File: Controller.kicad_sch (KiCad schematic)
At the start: 33 parts, among them J12 Conn_01x03_Pin, J2 Conn_01x04_Pin, J3 Conn_01x02_Pin, J4 Conn_01x02_Pin, J5 Conn_01x04_Pin, J6 Conn_01x02_Pin, SW1 SW_Push, U1 STM32F407VETx, U6 TL431M-0.3%-6AF, Y1 8M, Y2 32.768K

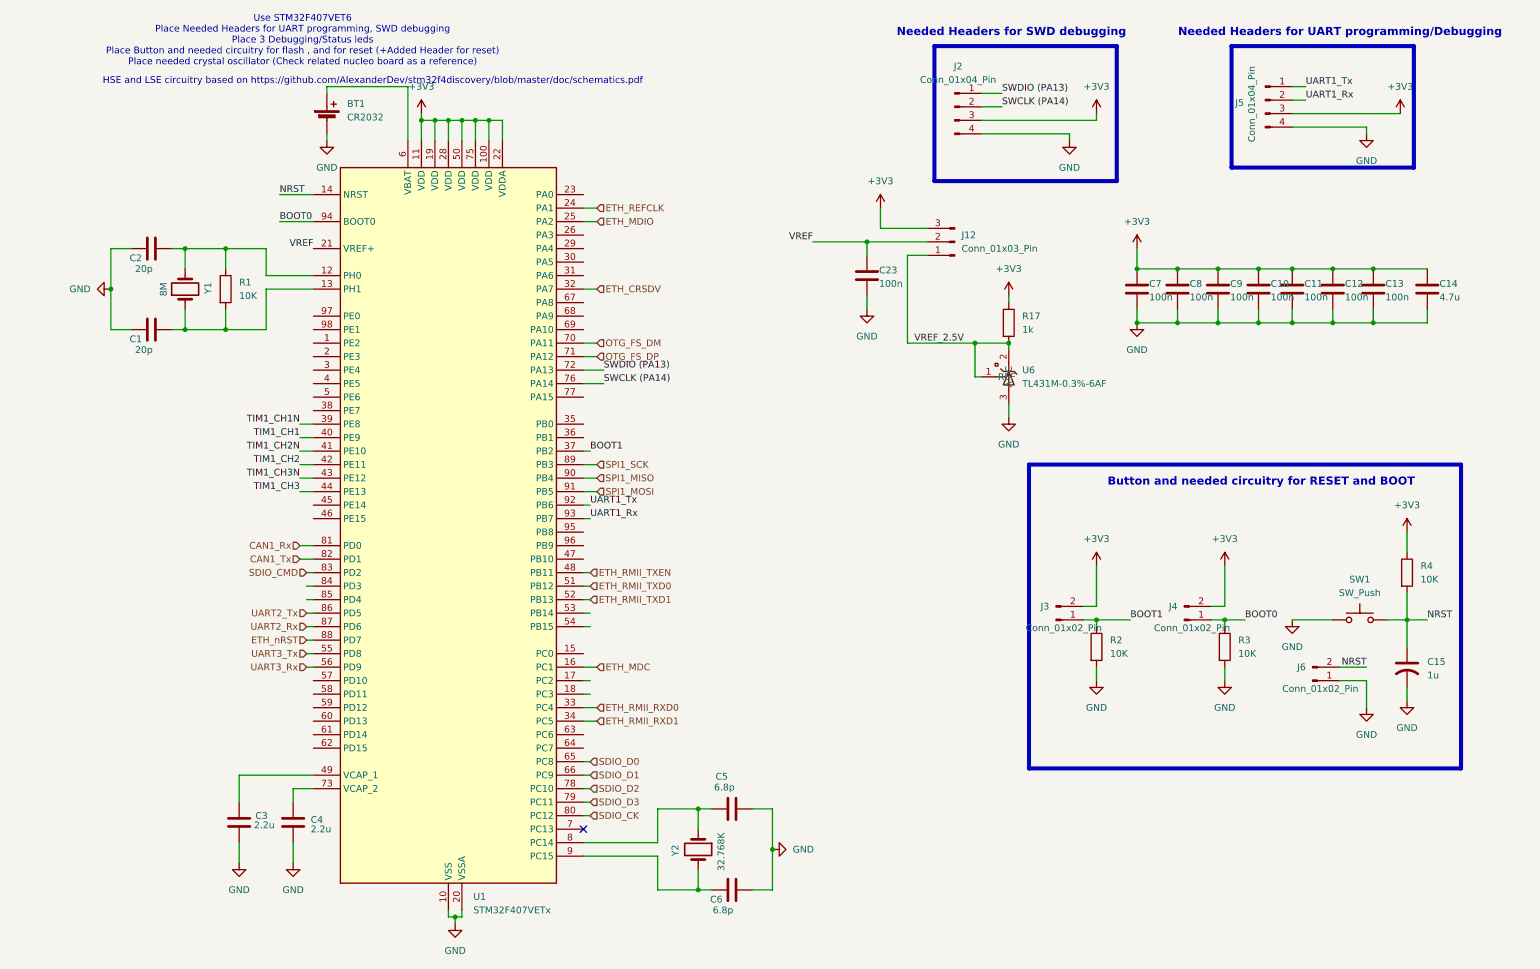
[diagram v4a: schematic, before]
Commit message: Schematic--Footprint link
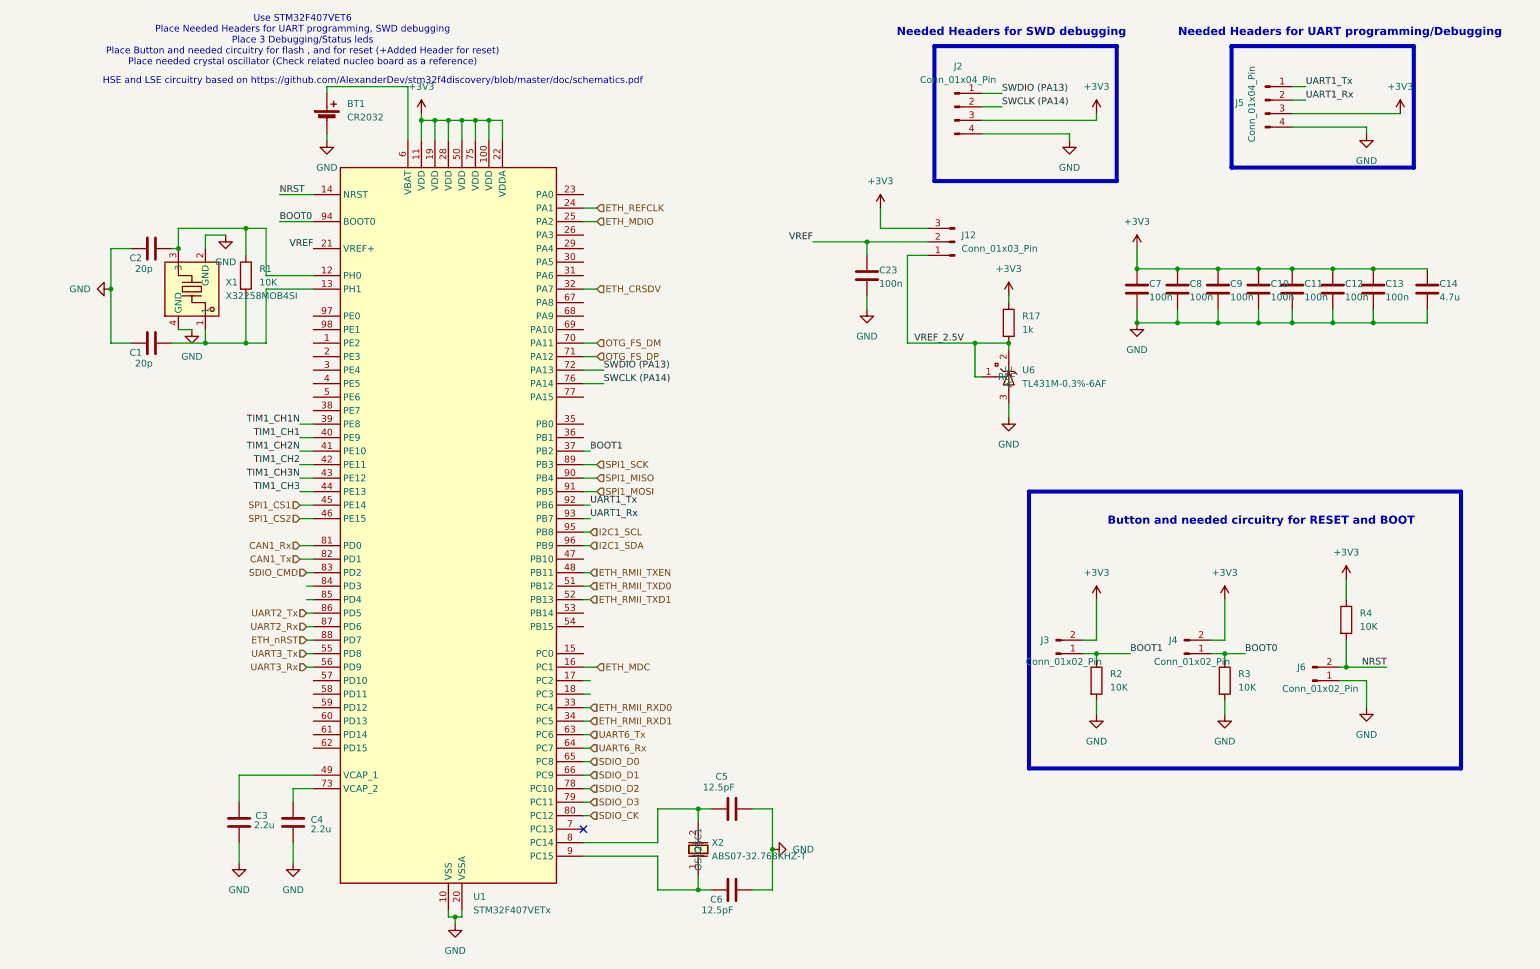
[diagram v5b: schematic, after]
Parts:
- removed C15: 1u, symbol Device:C_US
- removed SW1: SW_Push, symbol Switch:SW_Push
- removed Y1: 8M, symbol Device:Crystal
- removed Y2: 32.768K, symbol Device:Crystal
- added X1: X32258MOB4SI, EasyEDA:CRYSTAL-SMD_4P-L3.2-W2.5-BL, symbol EasyEDA:X32258MOB4SI
- added X2: ABS07-32.768KHZ-T, EasyEDA:OSC-SMD_2P-L3.2-W1.5, symbol EasyEDA:ABS07-32.768KHZ-T
- C1, C10, C11, C12, C13, C14, C2, C23, C3, C4, C7, C8, C9: footprint (none) -> Capacitor_SMD:C_0805_2012Metric
- C5, C6: value 6.8p -> 12.5pF; footprint (none) -> Capacitor_SMD:C_0805_2012Metric
- J12: footprint (none) -> Connector_PinHeader_2.54mm:PinHeader_1x03_P2.54mm_Vertical
- J2, J5: footprint (none) -> Connector_PinHeader_2.54mm:PinHeader_1x04_P2.54mm_Vertical
- J3, J4, J6: footprint (none) -> Connector_PinHeader_2.54mm:PinHeader_1x02_P2.54mm_Vertical
- R1, R17, R2, R3, R4: footprint (none) -> Resistor_SMD:R_0805_2012Metric
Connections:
- net GND: now also X1.2 (GND), X1.4 (GND)
- net at C2.2, R1.1, U1.12 (PH0): now also X1.3
- net at C1.2, R1.2, U1.13 (PH1): now also X1.1
- net at C5.1, U1.8 (PC14): now also X2.2 (OSC2)
- net at C6.1, U1.9 (PC15): now also X2.1 (OSC1)
- net SPI1_CS1: now reaches U1.45 (PE14)
- net SPI1_CS2: now reaches U1.46 (PE15)
- net UART6_Tx: now reaches U1.63 (PC6)
- net UART6_Rx: now reaches U1.64 (PC7)
- net I2C1_SCL: now reaches U1.95 (PB8)
- net I2C1_SDA: now reaches U1.96 (PB9)
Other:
- moved on the sheet: C1, J3, J4, R1, R2, R3, R4
